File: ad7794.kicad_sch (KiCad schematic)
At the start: 4 parts, among them U1101 AD7794BRUZ

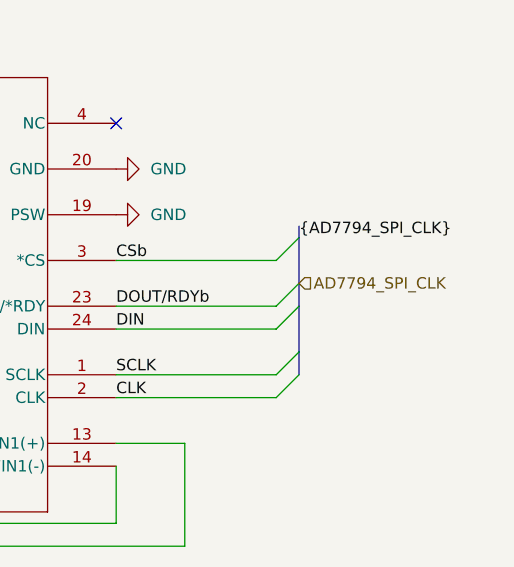
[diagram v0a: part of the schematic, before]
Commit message: Updates from Michal to fix ERC errors
Still lots of ERC warnings
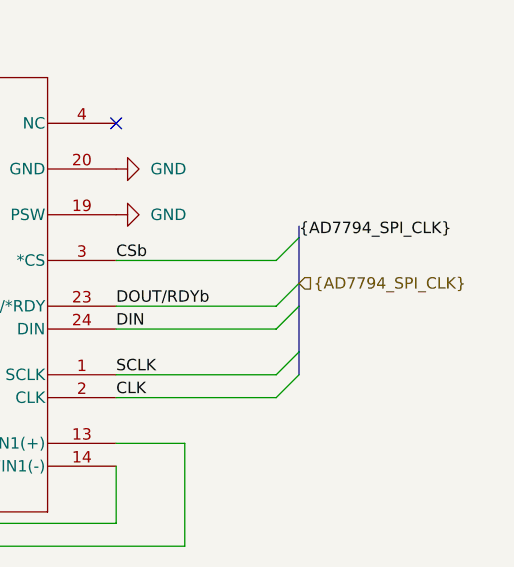
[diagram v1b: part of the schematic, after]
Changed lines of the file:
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@@
 		)
 	)
-	(hierarchical_label "AD7794_SPI_CLK"
+	(hierarchical_label "{AD7794_SPI_CLK}"
 		(shape input)
 		(at 248.92 95.25 0)

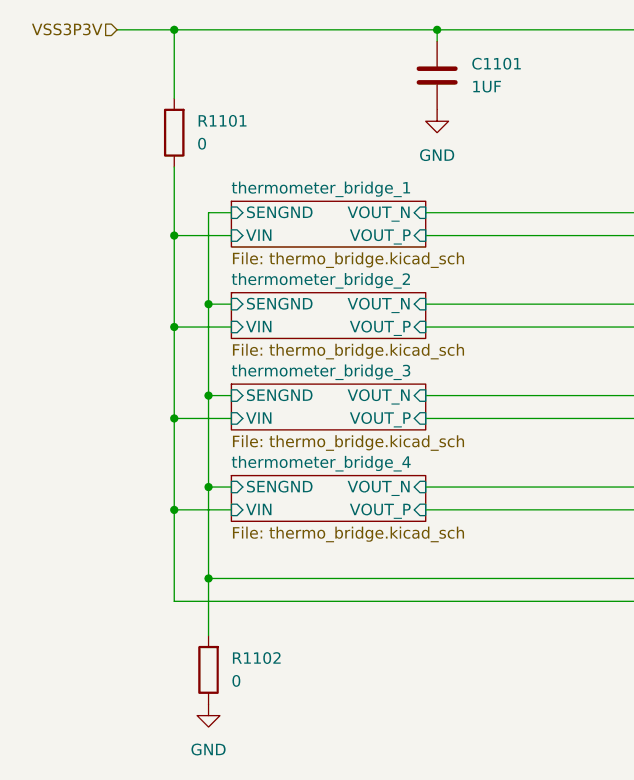
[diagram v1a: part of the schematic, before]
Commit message: Schematic Changes
Added Manufacturer/MPN/Description Fields to parts
Added libraries to project
Modified FMC schematic to use new symbol
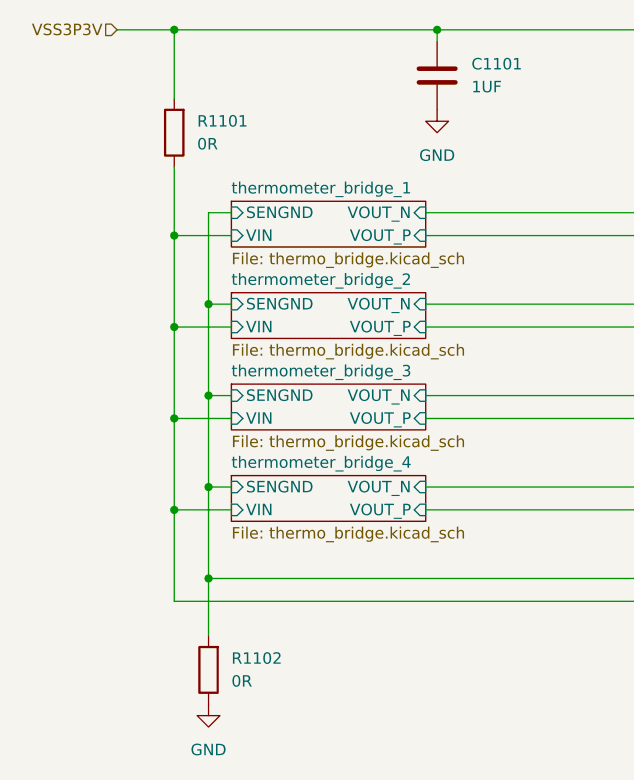
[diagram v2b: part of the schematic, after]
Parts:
- C1101: Manufacturer (none) -> Murata; Manufacturer Part Number (none) -> GRM188R61E105KA12D
- R1101, R1102: value 0 -> 0R; Manufacturer (none) -> Panasonic; Manufacturer Part Number (none) -> ERJ-3GEY0R00V
- U1101: Manufacturer (none) -> Analog Devices; Manufacturer Part Number (none) -> AD7794BRUZ
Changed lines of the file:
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@@
 			)
 		)
-		(property "Description" ""
+		(property "Description" "IC ADC 24BIT SIGMA-DELTA 24TSSOP"
 			(at 147.32 77.47 0)
 			(effects
@@
 		(property "Vendor" "digikey:AD7794BRUZ-ND"
 			(at 0 154.94 0)
+			(effects
+				(font
+					(size 1.27 1.27)
+				)
+				(hide yes)
+			)
+		)
+		(property "Manufacturer" "Analog Devices"
+			(at 147.32 77.47 0)
+			(effects
+				(font
+					(size 1.27 1.27)
+				)
+				(hide yes)
+			)
+		)
+		(property "Manufacturer Part Number" "AD7794BRUZ "
+			(at 147.32 77.47 0)
 			(effects
 				(font
@@
 			)
 		)
-		(property "Value" "0"
+		(property "Value" "0R"
 			(at 85.09 73.6599 0)
 			(effects
@@
 			)
 		)
-		(property "Description" "Resistor"
+		(property "Description" "RES SMD 0 OHM JUMPER 1/10W 0603"
 			(at 82.55 72.39 0)
 			(effects
@@
 		(property "Vendor" "digikey:P0.0GCT-ND"
 			(at 165.1 0 0)
+			(effects
+				(font
+					(size 1.27 1.27)
+				)
+				(hide yes)
+			)
+		)
+		(property "Manufacturer" "Panasonic"
+			(at 82.55 72.39 0)
+			(effects
+				(font
+					(size 1.27 1.27)
+				)
+				(hide yes)
+			)
+		)
+		(property "Manufacturer Part Number" "ERJ-3GEY0R00V "
+			(at 82.55 72.39 0)
 			(effects
 				(font
@@
 			)
 		)
-		(property "Value" "0"
+		(property "Value" "0R"
 			(at 88.9 133.3499 0)
 			(effects
@@
 			)
 		)
-		(property "Description" "Resistor"
+		(property "Description" "RES SMD 0 OHM JUMPER 1/10W 0603"
 			(at 86.36 132.08 0)
 			(effects
@@
 		(property "Vendor" "digikey:P0.0GCT-ND"
 			(at 172.72 0 0)
+			(effects
+				(font
+					(size 1.27 1.27)
+				)
+				(hide yes)
+			)
+		)
+		(property "Manufacturer" "Panasonic"
+			(at 86.36 132.08 0)
+			(effects
+				(font
+					(size 1.27 1.27)
+				)
+				(hide yes)
+			)
+		)
+		(property "Manufacturer Part Number" "ERJ-3GEY0R00V "
+			(at 86.36 132.08 0)
 			(effects
 				(font
@@
 			)
 		)
-		(property "Description" "Unpolarized capacitor"
+		(property "Description" "CAP CER 1UF 25V X5R 0603"
 			(at 111.76 66.04 0)
 			(effects
@@
 		(property "Vendor" "digikey:490-3897-1-ND"
 			(at 0 132.08 0)
+			(effects
+				(font
+					(size 1.27 1.27)
+				)
+				(hide yes)
+			)
+		)
+		(property "Manufacturer" "Murata"
+			(at 111.76 66.04 0)
+			(effects
+				(font
+					(size 1.27 1.27)
+				)
+				(hide yes)
+			)
+		)
+		(property "Manufacturer Part Number" "GRM188R61E105KA12D"
+			(at 111.76 66.04 0)
 			(effects
 				(font
@@
 			)
 		)
+		(instances
+			(project "zest"
+				(path "/00000000-0000-0000-0000-000000000003/00000000-0000-0000-0000-00000000000a"
+					(page "36")
+				)
+			)
+		)
 	)
 	(sheet
@@
 			)
 		)
+		(instances
+			(project "zest"
+				(path "/00000000-0000-0000-0000-000000000003/00000000-0000-0000-0000-00000000000a"
+					(page "33")
+				)
+			)
+		)
 	)
 	(sheet
@@
 			)
 		)
+		(instances
+			(project "zest"
+				(path "/00000000-0000-0000-0000-000000000003/00000000-0000-0000-0000-00000000000a"
+					(page "34")
+				)
+			)
+		)
 	)
 	(sheet
@@
 			)
 		)
+		(instances
+			(project "zest"
+				(path "/00000000-0000-0000-0000-000000000003/00000000-0000-0000-0000-00000000000a"
+					(page "35")
+				)
+			)
+		)

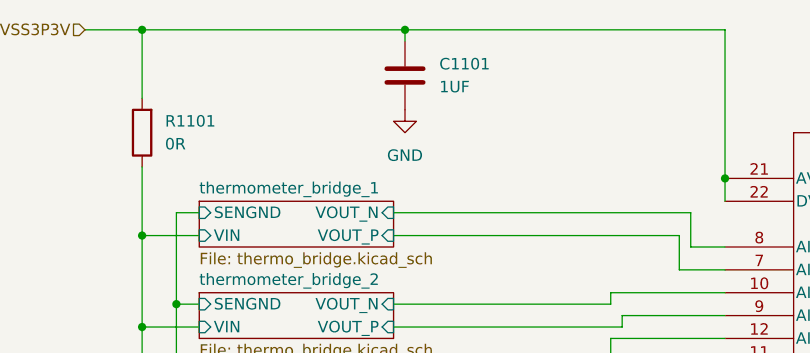
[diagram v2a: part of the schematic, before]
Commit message: Schematics update
Cleaned up RF ADC and front end sections.
Verified that changes did not changes anything about the layout.
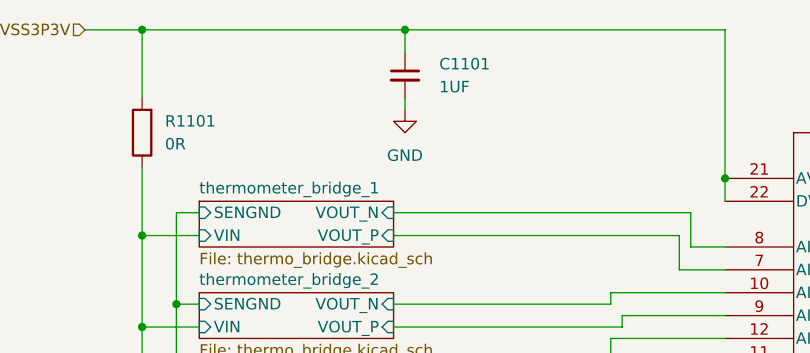
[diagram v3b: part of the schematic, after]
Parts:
- C1101: symbol Device:C -> Device:C_Small
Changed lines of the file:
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@@
 	(wire
 		(pts
-			(xy 111.76 60.96) (xy 111.76 62.23)
+			(xy 111.76 60.96) (xy 111.76 63.5)
 		)
 		(stroke
@@
 		(pts
 			(xy 82.55 60.96) (xy 111.76 60.96)
+		)
+		(stroke
+			(width 0)
+			(type default)
+		)
+	)
+	(wire
+		(pts
+			(xy 111.76 68.58) (xy 111.76 69.85)
 		)
 		(stroke
@@
 	)
 	(symbol
-		(lib_id "Device:C")
+		(lib_id "Device:C_Small")
 		(at 111.76 66.04 0)
 		(unit 1)
